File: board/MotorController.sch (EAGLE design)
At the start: 9 parts, among them IC1 7805TV, U1 ATTINY85-20P

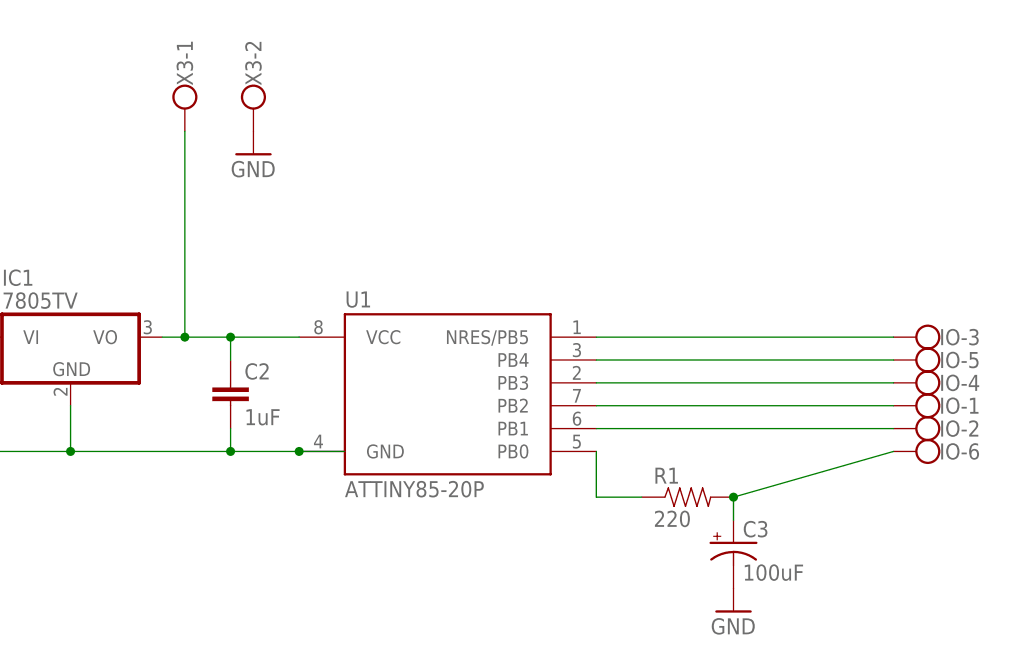
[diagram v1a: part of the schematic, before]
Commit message: Tweaked schematic
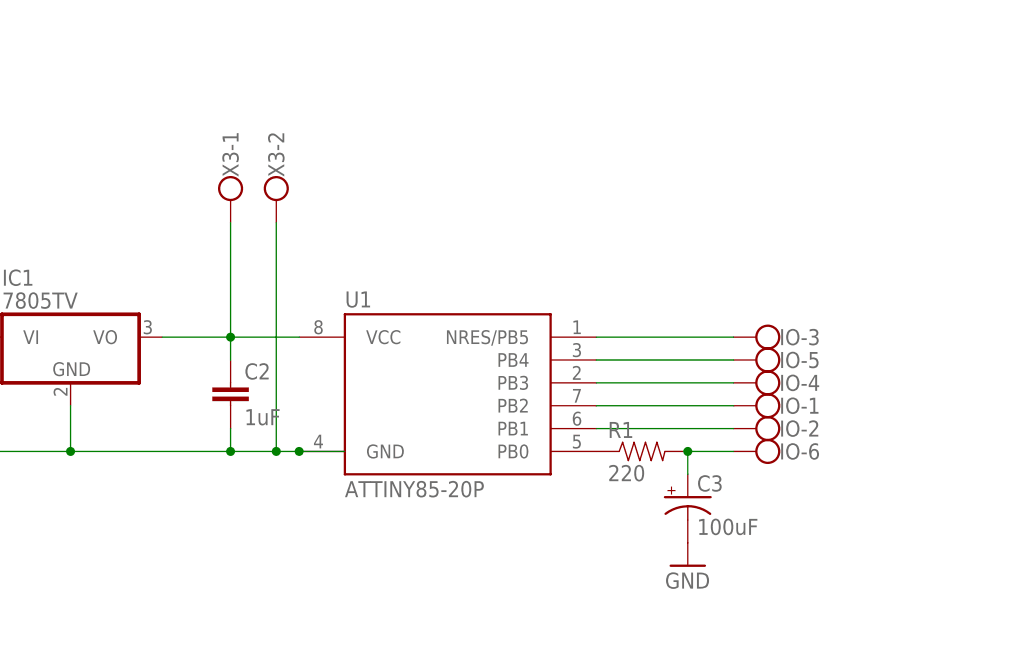
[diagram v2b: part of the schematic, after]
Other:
- moved on the sheet: C3, IO-1, IO-2, IO-3, IO-4, IO-5, IO-6, R1, X3-1, X3-2
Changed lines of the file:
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@@
 <part name="IO" library="con-wago-500" deviceset="W237-136" device=""/>
 <part name="X3" library="con-wago-500" deviceset="W237-102" device=""/>
-<part name="GND7" library="supply1" deviceset="GND" device=""/>
 <part name="C2" library="SparkFun-Capacitors" deviceset="CAP" device="PTH" value="1uF"/>
 </parts>
@@
 <instance part="IC1" gate="A1" x="0" y="63.5"/>
 <instance part="C1" gate="G$1" x="-17.78" y="58.42"/>
-<instance part="C3" gate="G$1" x="73.66" y="40.64"/>
-<instance part="R1" gate="G$1" x="68.58" y="45.72"/>
-<instance part="GND5" gate="1" x="73.66" y="33.02"/>
+<instance part="C3" gate="G$1" x="68.58" y="45.72"/>
+<instance part="R1" gate="G$1" x="63.5" y="50.8"/>
+<instance part="GND5" gate="1" x="68.58" y="38.1"/>
 <instance part="24V" gate="-1" x="-30.48" y="63.5"/>
 <instance part="24V" gate="-2" x="-30.48" y="50.8"/>
-<instance part="IO" gate="-1" x="96.52" y="55.88" rot="R180"/>
-<instance part="IO" gate="-2" x="96.52" y="53.34" rot="R180"/>
-<instance part="IO" gate="-3" x="96.52" y="63.5" rot="R180"/>
-<instance part="IO" gate="-4" x="96.52" y="58.42" rot="R180"/>
-<instance part="IO" gate="-5" x="96.52" y="60.96" rot="R180"/>
-<instance part="IO" gate="-6" x="96.52" y="50.8" rot="R180"/>
-<instance part="X3" gate="-1" x="12.7" y="91.44" rot="R270"/>
-<instance part="X3" gate="-2" x="20.32" y="91.44" rot="R270"/>
-<instance part="GND7" gate="1" x="20.32" y="83.82"/>
+<instance part="IO" gate="-1" x="78.74" y="55.88" rot="R180"/>
+<instance part="IO" gate="-2" x="78.74" y="53.34" rot="R180"/>
+<instance part="IO" gate="-3" x="78.74" y="63.5" rot="R180"/>
+<instance part="IO" gate="-4" x="78.74" y="58.42" rot="R180"/>
+<instance part="IO" gate="-5" x="78.74" y="60.96" rot="R180"/>
+<instance part="IO" gate="-6" x="78.74" y="50.8" rot="R180"/>
+<instance part="X3" gate="-1" x="17.78" y="81.28" rot="R270"/>
+<instance part="X3" gate="-2" x="22.86" y="81.28" rot="R270"/>
 <instance part="C2" gate="G$1" x="17.78" y="55.88"/>
 </instances>
@@
 <pinref part="R1" gate="G$1" pin="2"/>
 <pinref part="C3" gate="G$1" pin="+"/>
-<wire x1="73.66" y1="43.18" x2="73.66" y2="45.72" width="0.1524" layer="91"/>
+<wire x1="68.58" y1="48.26" x2="68.58" y2="50.8" width="0.1524" layer="91"/>
 <pinref part="IO" gate="-6" pin="KL"/>
-<wire x1="91.44" y1="50.8" x2="73.66" y2="45.72" width="0.1524" layer="91"/>
-<junction x="73.66" y="45.72"/>
+<wire x1="73.66" y1="50.8" x2="68.58" y2="50.8" width="0.1524" layer="91"/>
+<junction x="68.58" y="50.8"/>
 </segment>
 </net>
@@
 <pinref part="C3" gate="G$1" pin="-"/>
 <pinref part="GND5" gate="1" pin="GND"/>
-</segment>
-<segment>
-<pinref part="X3" gate="-2" pin="KL"/>
-<pinref part="GND7" gate="1" pin="GND"/>
 </segment>
 <segment>
@@
 <pinref part="U1" gate="G$1" pin="GND"/>
 <wire x1="25.4" y1="50.8" x2="30.48" y2="50.8" width="0.1524" layer="91"/>
-<wire x1="25.4" y1="50.8" x2="17.78" y2="50.8" width="0.1524" layer="91"/>
+<wire x1="25.4" y1="50.8" x2="22.86" y2="50.8" width="0.1524" layer="91"/>
 <junction x="0" y="50.8"/>
 <pinref part="C1" gate="G$1" pin="-"/>
+<wire x1="22.86" y1="50.8" x2="17.78" y2="50.8" width="0.1524" layer="91"/>
 <wire x1="17.78" y1="50.8" x2="0" y2="50.8" width="0.1524" layer="91"/>
 <wire x1="-17.78" y1="53.34" x2="-17.78" y2="50.8" width="0.1524" layer="91"/>
@@
 <wire x1="17.78" y1="53.34" x2="17.78" y2="50.8" width="0.1524" layer="91"/>
 <junction x="17.78" y="50.8"/>
+<pinref part="C2" gate="G$1" pin="2"/>
+<pinref part="X3" gate="-2" pin="KL"/>
+<wire x1="22.86" y1="76.2" x2="22.86" y2="50.8" width="0.1524" layer="91"/>
+<junction x="22.86" y="50.8"/>
 <junction x="25.4" y="50.8"/>
-<pinref part="C2" gate="G$1" pin="2"/>
 </segment>
 </net>
@@
 <pinref part="R1" gate="G$1" pin="1"/>
 <pinref part="U1" gate="G$1" pin="PB0"/>
-<wire x1="63.5" y1="45.72" x2="58.42" y2="45.72" width="0.1524" layer="91"/>
-<wire x1="58.42" y1="45.72" x2="58.42" y2="50.8" width="0.1524" layer="91"/>
 </segment>
 </net>
@@
 <pinref part="IC1" gate="A1" pin="VO"/>
 <wire x1="25.4" y1="63.5" x2="17.78" y2="63.5" width="0.1524" layer="91"/>
-<pinref part="X3" gate="-1" pin="KL"/>
-<wire x1="17.78" y1="63.5" x2="12.7" y2="63.5" width="0.1524" layer="91"/>
-<wire x1="12.7" y1="63.5" x2="10.16" y2="63.5" width="0.1524" layer="91"/>
-<wire x1="12.7" y1="86.36" x2="12.7" y2="63.5" width="0.1524" layer="91"/>
-<junction x="12.7" y="63.5"/>
+<wire x1="17.78" y1="63.5" x2="10.16" y2="63.5" width="0.1524" layer="91"/>
 <wire x1="17.78" y1="60.96" x2="17.78" y2="63.5" width="0.1524" layer="91"/>
 <junction x="17.78" y="63.5"/>
 <pinref part="C2" gate="G$1" pin="1"/>
+<pinref part="X3" gate="-1" pin="KL"/>
+<wire x1="17.78" y1="76.2" x2="17.78" y2="63.5" width="0.1524" layer="91"/>
 </segment>
 </net>
@@
 <pinref part="U1" gate="G$1" pin="NRES/PB5"/>
 <pinref part="IO" gate="-3" pin="KL"/>
-<wire x1="58.42" y1="63.5" x2="91.44" y2="63.5" width="0.1524" layer="91"/>
+<wire x1="58.42" y1="63.5" x2="73.66" y2="63.5" width="0.1524" layer="91"/>
 </segment>
 </net>
@@
 <pinref part="IO" gate="-4" pin="KL"/>
 <pinref part="U1" gate="G$1" pin="PB3"/>
-<wire x1="91.44" y1="58.42" x2="58.42" y2="58.42" width="0.1524" layer="91"/>
+<wire x1="73.66" y1="58.42" x2="58.42" y2="58.42" width="0.1524" layer="91"/>
 </segment>
 </net>
@@
 <pinref part="U1" gate="G$1" pin="PB4"/>
 <pinref part="IO" gate="-5" pin="KL"/>
-<wire x1="58.42" y1="60.96" x2="91.44" y2="60.96" width="0.1524" layer="91"/>
+<wire x1="58.42" y1="60.96" x2="73.66" y2="60.96" width="0.1524" layer="91"/>
 </segment>
 </net>
@@
 <pinref part="U1" gate="G$1" pin="PB2"/>
 <pinref part="IO" gate="-1" pin="KL"/>
-<wire x1="58.42" y1="55.88" x2="91.44" y2="55.88" width="0.1524" layer="91"/>
+<wire x1="58.42" y1="55.88" x2="73.66" y2="55.88" width="0.1524" layer="91"/>
 </segment>
 </net>
@@
 <pinref part="U1" gate="G$1" pin="PB1"/>
 <pinref part="IO" gate="-2" pin="KL"/>
-<wire x1="58.42" y1="53.34" x2="91.44" y2="53.34" width="0.1524" layer="91"/>
+<wire x1="58.42" y1="53.34" x2="73.66" y2="53.34" width="0.1524" layer="91"/>
 </segment>
 </net>

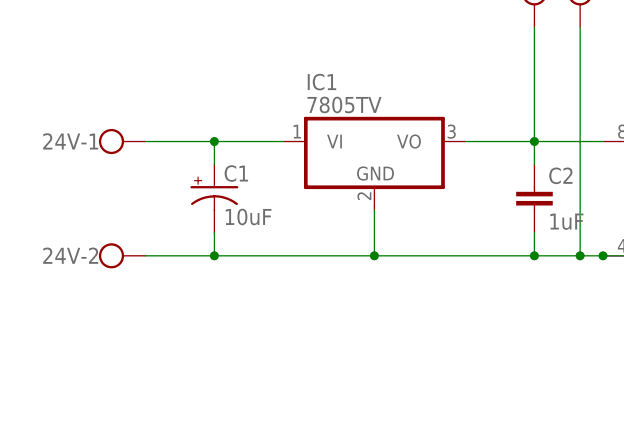
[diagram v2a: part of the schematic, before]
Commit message: Switch to a top GND pour
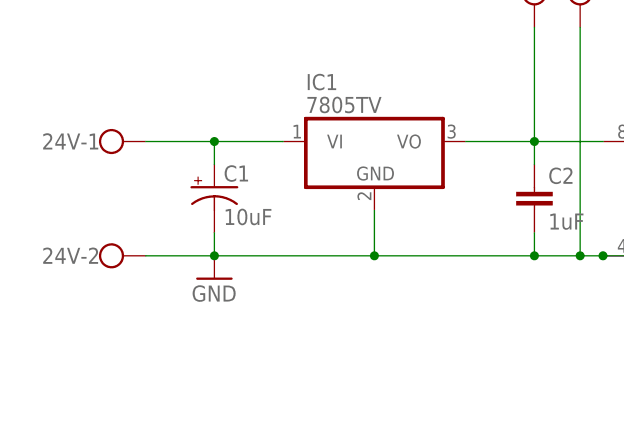
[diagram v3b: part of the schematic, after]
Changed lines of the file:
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@@
 <part name="X3" library="con-wago-500" deviceset="W237-102" device=""/>
 <part name="C2" library="SparkFun-Capacitors" deviceset="CAP" device="PTH" value="1uF"/>
+<part name="GND1" library="supply1" deviceset="GND" device=""/>
 </parts>
 <sheets>
@@
 <instance part="X3" gate="-2" x="22.86" y="81.28" rot="R270"/>
 <instance part="C2" gate="G$1" x="17.78" y="55.88"/>
+<instance part="GND1" gate="1" x="-17.78" y="48.26"/>
 </instances>
 <busses>
@@
 <junction x="22.86" y="50.8"/>
 <junction x="25.4" y="50.8"/>
+<pinref part="GND1" gate="1" pin="GND"/>
 </segment>
 </net>

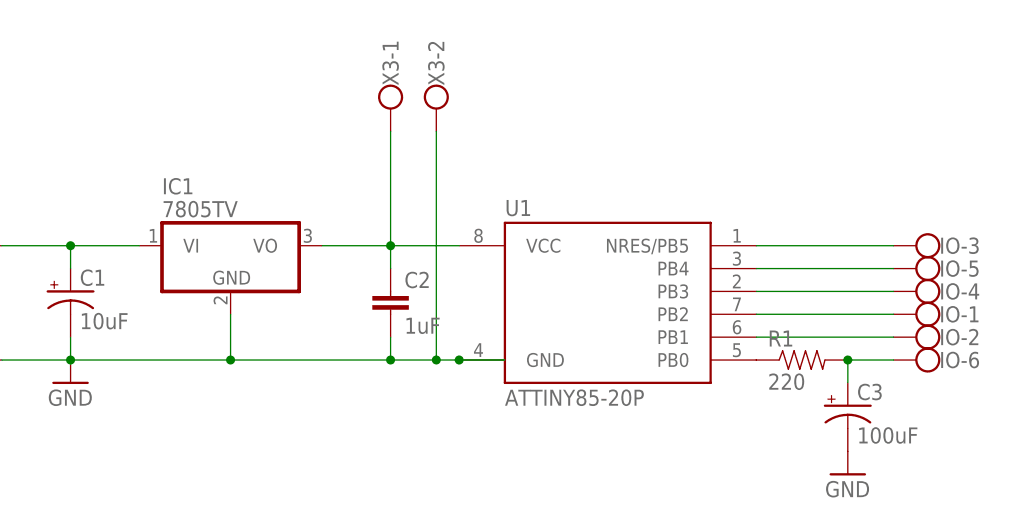
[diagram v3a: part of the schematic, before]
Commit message: Switch to a horizontal regulator and change board layout to fit
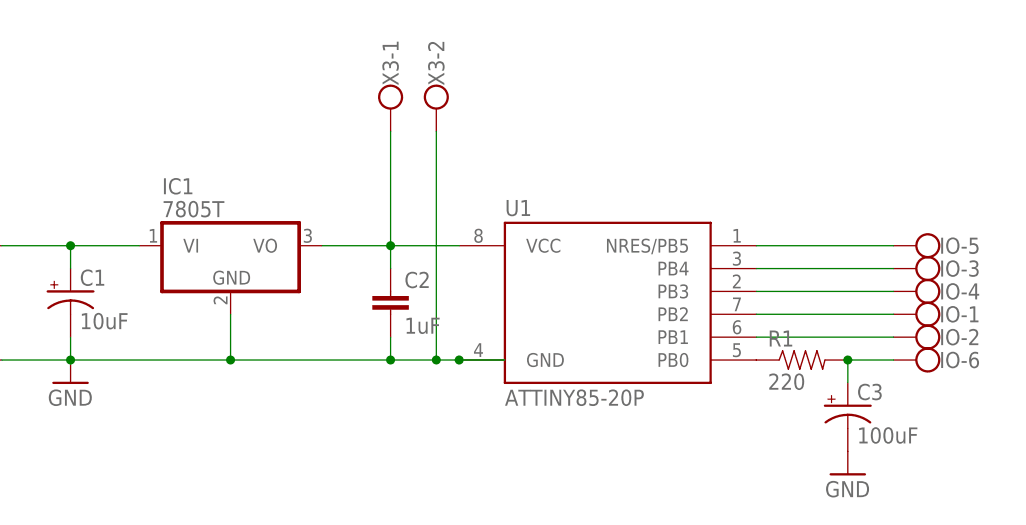
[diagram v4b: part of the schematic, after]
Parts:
- IC1: value 7805TV -> 7805T; device linear:7805TV -> linear:7805T
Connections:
- removed net N$4 (its old number): IO-5.KL, U1.PB4
- removed net N$5 (its old number): IO-3.KL, U1.NRES/PB5
- new net N$1: IO-3.KL, U1.PB4
- new net N$3: IO-5.KL, U1.NRES/PB5
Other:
- moved on the sheet: IO-3, IO-5
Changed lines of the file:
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@@
 <parts>
 <part name="U1" library="_hhn_attiny25_45_85" deviceset="ATTINY85*" device="P" technology="-20"/>
-<part name="IC1" library="linear" deviceset="78*" device="TV" technology="05"/>
+<part name="IC1" library="linear" deviceset="78*" device="T" technology="05" value="7805T"/>
 <part name="C1" library="SparkFun-Capacitors" deviceset="CAP_POL" device="PTH2" value="10uF"/>
 <part name="C3" library="SparkFun-Capacitors" deviceset="CAP_POL" device="PTH2" value="100uF"/>
@@
 <instance part="IO" gate="-1" x="78.74" y="55.88" rot="R180"/>
 <instance part="IO" gate="-2" x="78.74" y="53.34" rot="R180"/>
-<instance part="IO" gate="-3" x="78.74" y="63.5" rot="R180"/>
+<instance part="IO" gate="-3" x="78.74" y="60.96" rot="R180"/>
 <instance part="IO" gate="-4" x="78.74" y="58.42" rot="R180"/>
-<instance part="IO" gate="-5" x="78.74" y="60.96" rot="R180"/>
+<instance part="IO" gate="-5" x="78.74" y="63.5" rot="R180"/>
 <instance part="IO" gate="-6" x="78.74" y="50.8" rot="R180"/>
 <instance part="X3" gate="-1" x="17.78" y="81.28" rot="R270"/>
@@
 </segment>
 </net>
+<net name="N$4" class="0">
+<segment>
+<pinref part="U1" gate="G$1" pin="PB2"/>
+<pinref part="IO" gate="-1" pin="KL"/>
+<wire x1="58.42" y1="55.88" x2="73.66" y2="55.88" width="0.1524" layer="91"/>
+</segment>
+</net>
 <net name="N$5" class="0">
 <segment>
-<pinref part="U1" gate="G$1" pin="NRES/PB5"/>
-<pinref part="IO" gate="-3" pin="KL"/>
-<wire x1="58.42" y1="63.5" x2="73.66" y2="63.5" width="0.1524" layer="91"/>
+<pinref part="IO" gate="-2" pin="KL"/>
+<pinref part="U1" gate="G$1" pin="PB1"/>
+<wire x1="73.66" y1="53.34" x2="58.42" y2="53.34" width="0.1524" layer="91"/>
 </segment>
 </net>
-<net name="N$3" class="0">
+<net name="N$1" class="0">
+<segment>
+<pinref part="U1" gate="G$1" pin="PB4"/>
+<pinref part="IO" gate="-3" pin="KL"/>
+<wire x1="58.42" y1="60.96" x2="73.66" y2="60.96" width="0.1524" layer="91"/>
+</segment>
+</net>
+<net name="N$2" class="0">
 <segment>
 <pinref part="IO" gate="-4" pin="KL"/>
@@
 </segment>
 </net>
-<net name="N$4" class="0">
+<net name="N$3" class="0">
 <segment>
-<pinref part="U1" gate="G$1" pin="PB4"/>
+<pinref part="U1" gate="G$1" pin="NRES/PB5"/>
 <pinref part="IO" gate="-5" pin="KL"/>
-<wire x1="58.42" y1="60.96" x2="73.66" y2="60.96" width="0.1524" layer="91"/>
+<wire x1="58.42" y1="63.5" x2="73.66" y2="63.5" width="0.1524" layer="91"/>
 </segment>
 </net>
-<net name="N$1" class="0">
-<segment>
-<pinref part="U1" gate="G$1" pin="PB2"/>
-<pinref part="IO" gate="-1" pin="KL"/>
-<wire x1="58.42" y1="55.88" x2="73.66" y2="55.88" width="0.1524" layer="91"/>
-</segment>
-</net>
-<net name="N$2" class="0">
-<segment>
-<pinref part="U1" gate="G$1" pin="PB1"/>
-<pinref part="IO" gate="-2" pin="KL"/>
-<wire x1="58.42" y1="53.34" x2="73.66" y2="53.34" width="0.1524" layer="91"/>
-</segment>
-</net>

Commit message: Changes
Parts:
- removed IO: (no value), con-wago-500:W237-136
- added C4, C6: 1uF, SparkFun-Capacitors:CAPPTH1
- added R2: 220R, SparkFun-Resistors:RESISTORAXIAL-0.3
- added X1, X2, X4: (no value), con-wago-500:W237-103
- C1: value 10uF -> 1uF; device SparkFun-Capacitors:CAP_POLPTH2 -> SparkFun-Capacitors:CAPPTH1
- C2: value 1uF -> 0.1uF; device SparkFun-Capacitors:CAPPTH -> SparkFun-Capacitors:CAPPTH1
- C3: value 100uF -> 1uF; device SparkFun-Capacitors:CAP_POLPTH2 -> SparkFun-Capacitors:CAPPTH1
- R1: value 220 -> 220R
- U1: value ATTINY85-20P -> ATTINY84-20PU; device _hhn_attiny25_45_85:ATTINY85-20P -> Atmel_By_element14_Batch_1:ATTINY84-20PU
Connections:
- removed net N$3: IO-5.KL, U1.NRES/PB5
- removed net N$4: IO-1.KL, U1.PB2
- removed net N$5: IO-2.KL, U1.PB1
- removed net N$6: R1.1, U1.PB0
- removed net VSPD: C3.+, IO-6.KL, R1.2
- new net DIR_IN: U1.PA2, X2-1.KL
- new net DIR_OUT: U1.PA7, X4-2.KL
- new net I2C_SCL: U1.PA4, X1-2.KL
- new net I2C_SDA: U1.PA6, X4-1.KL
- new net RAMP_IN: U1.PA1, X2-2.KL
- new net RPM_IN: U1.PB2, X4-3.KL
- new net SPD_IN: U1.PA0, X2-3.KL
- new net SPD_OUT: R1.2, U1.PA5
- new net START_IN: U1.PA3, X1-3.KL
- net +24V: now also C1.2; no longer C1.+
- net GND: now also C1.1, C3.2, C4.1, C6.1; no longer C1.-, C3.-
- net N$1: now also C6.2, R1.1, R2.1; no longer IO-3.KL, U1.PB4
- net N$2: now also C3.1, R2.2, X1-1.KL; no longer IO-4.KL, U1.PB3
- net VCC: now also C4.2
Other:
- moved on the sheet: R1
